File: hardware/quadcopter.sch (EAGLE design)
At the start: 62 parts, among them J1 AVR_SPI_PRG_6NS, J2 HEADER-4POS-2X2-0.1IN-FEMALE-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, J3 HEADER-10POSTH-254X10, J4 HEADER-4POS-0.1IN-FEMALE-SMD-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, Q1 MOSFET-SI2302CDS-T1-E3CT-ND, Q2 MOSFET-SI2302CDS-T1-E3CT-ND, Q3 MOSFET-SI2302CDS-T1-E3CT-ND, Q4 MOSFET-SI2302CDS-T1-E3CT-ND, Q5 MOSFET-SI2302CDS-T1-E3CT-ND, Q6 MOSFET-SI2302CDS-T1-E3CT-ND, SW1 PUSHBUTTON_SMD-VERTICAL-1, U1 ATMEGA128RFA1, U2 LSM-IMU-497-18367-1-NDIMU, Y1 CRYSTAL5X3

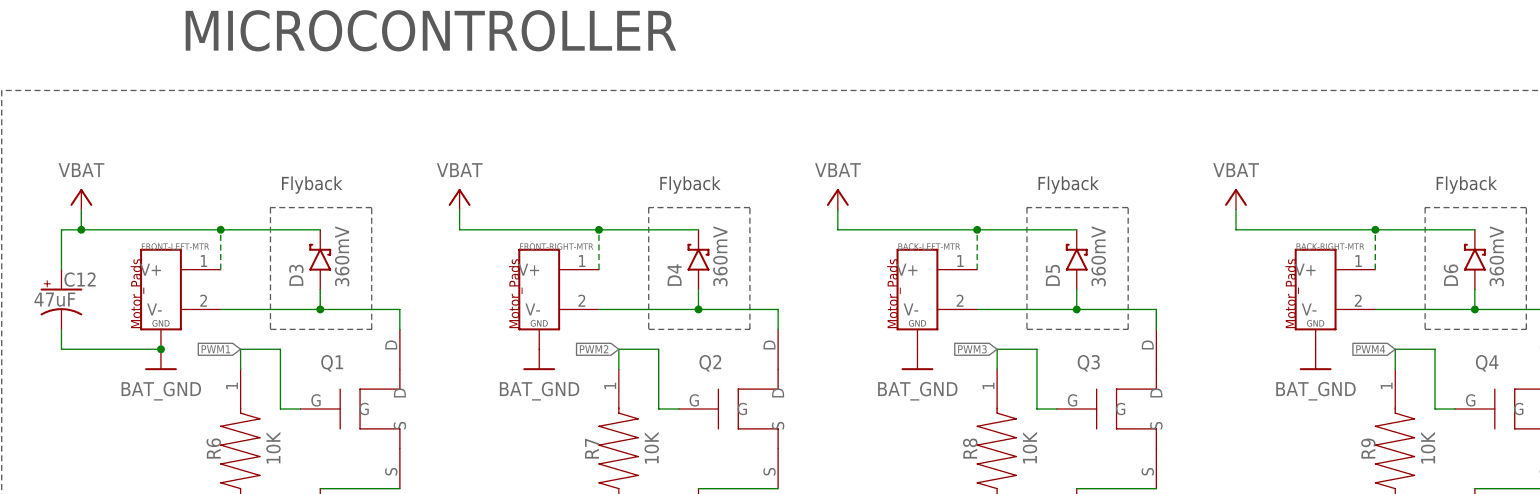
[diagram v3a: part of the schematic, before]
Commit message: renamed motor pads because mosfet is complaining?
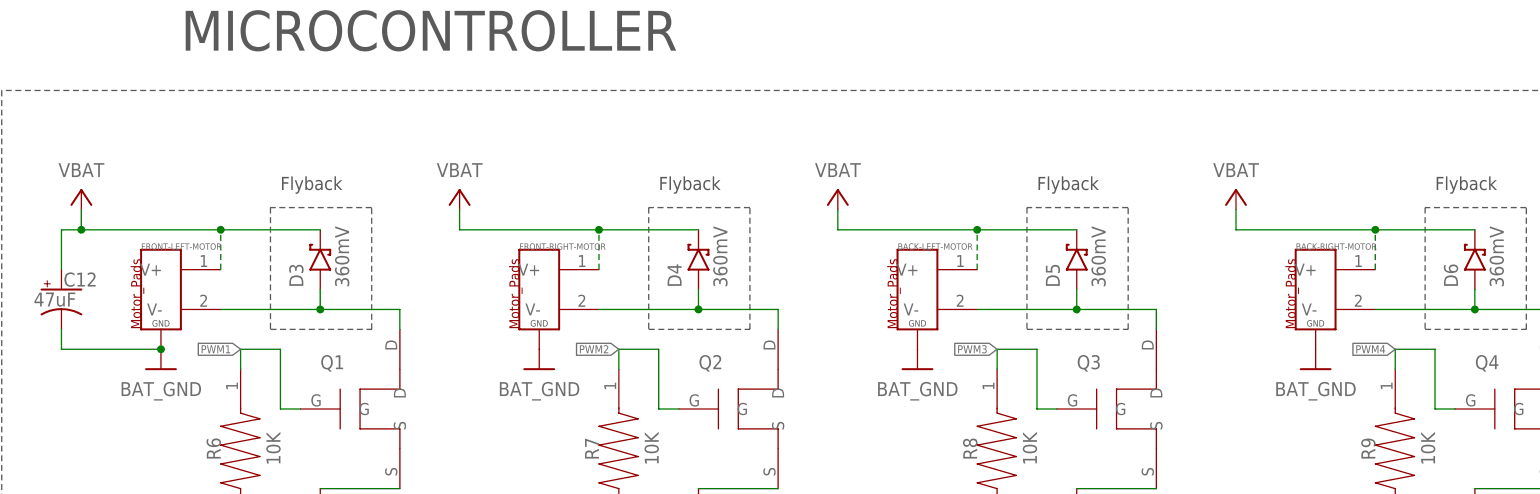
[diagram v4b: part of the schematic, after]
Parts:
- renumbered BACK-LEFT-MTR to BACK-LEFT-MOTOR, BACK-RIGHT-MTR to BACK-RIGHT-MOTOR, FRONT-LEFT-MTR to FRONT-LEFT-MOTOR, FRONT-RIGHT-MTR to FRONT-RIGHT-MOTOR
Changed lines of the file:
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@@
 <part name="GND18" library="quadparts_prebuilt_2022" deviceset="GND" device=""/>
 <part name="P+7" library="quadparts_prebuilt_2022" deviceset="3V" device=""/>
-<part name="FRONT-LEFT-MTR" library="quadparts_prebuilt_2022" deviceset="MOTOR_PADS_GND" device="-MOLEX-SMD"/>
+<part name="FRONT-LEFT-MOTOR" library="quadparts_prebuilt_2022" deviceset="MOTOR_PADS_GND" device="-MOLEX-SMD"/>
 <part name="P+8" library="quadparts_prebuilt_2022" deviceset="VBAT" device=""/>
 <part name="D3" library="quadparts_prebuilt_2022" deviceset="DIODE-SCHOTTKY_" device="-SMD-SOD123" package3d_urn="urn:adsk.eagle:package:11793366/1" value="360mV"/>
@@
 <part name="GND22" library="quadparts_prebuilt_2022" deviceset="GND" device=""/>
 <part name="Q1" library="custom_.lbr" library_urn="urn:adsk.wipprod:fs.file:vf.FjMADskDQ2Se9fX1PD5xcw" deviceset="MOSFET" device="-SI2302CDS-T1-E3CT-ND"/>
-<part name="FRONT-RIGHT-MTR" library="quadparts_prebuilt_2022" deviceset="MOTOR_PADS_GND" device="-MOLEX-SMD"/>
+<part name="FRONT-RIGHT-MOTOR" library="quadparts_prebuilt_2022" deviceset="MOTOR_PADS_GND" device="-MOLEX-SMD"/>
 <part name="P+9" library="quadparts_prebuilt_2022" deviceset="VBAT" device=""/>
 <part name="D4" library="quadparts_prebuilt_2022" deviceset="DIODE-SCHOTTKY_" device="-SMD-SOD123" package3d_urn="urn:adsk.eagle:package:11793366/1" value="360mV"/>
@@
 <part name="GND25" library="quadparts_prebuilt_2022" deviceset="GND" device=""/>
 <part name="Q2" library="custom_.lbr" library_urn="urn:adsk.wipprod:fs.file:vf.FjMADskDQ2Se9fX1PD5xcw" deviceset="MOSFET" device="-SI2302CDS-T1-E3CT-ND"/>
-<part name="BACK-LEFT-MTR" library="quadparts_prebuilt_2022" deviceset="MOTOR_PADS_GND" device="-MOLEX-SMD"/>
+<part name="BACK-LEFT-MOTOR" library="quadparts_prebuilt_2022" deviceset="MOTOR_PADS_GND" device="-MOLEX-SMD"/>
 <part name="P+10" library="quadparts_prebuilt_2022" deviceset="VBAT" device=""/>
 <part name="D5" library="quadparts_prebuilt_2022" deviceset="DIODE-SCHOTTKY_" device="-SMD-SOD123" package3d_urn="urn:adsk.eagle:package:11793366/1" value="360mV"/>
@@
 <part name="GND28" library="quadparts_prebuilt_2022" deviceset="GND" device=""/>
 <part name="Q3" library="custom_.lbr" library_urn="urn:adsk.wipprod:fs.file:vf.FjMADskDQ2Se9fX1PD5xcw" deviceset="MOSFET" device="-SI2302CDS-T1-E3CT-ND"/>
-<part name="BACK-RIGHT-MTR" library="quadparts_prebuilt_2022" deviceset="MOTOR_PADS_GND" device="-MOLEX-SMD"/>
+<part name="BACK-RIGHT-MOTOR" library="quadparts_prebuilt_2022" deviceset="MOTOR_PADS_GND" device="-MOLEX-SMD"/>
 <part name="P+11" library="quadparts_prebuilt_2022" deviceset="VBAT" device=""/>
 <part name="D6" library="quadparts_prebuilt_2022" deviceset="DIODE-SCHOTTKY_" device="-SMD-SOD123" package3d_urn="urn:adsk.eagle:package:11793366/1" value="360mV"/>
@@
 <attribute name="VALUE" x="287.02" y="162.56" size="1.778" layer="96" rot="R180" align="center"/>
 </instance>
-<instance part="FRONT-LEFT-MTR" gate="G$1" x="7.62" y="27.94" smashed="yes">
+<instance part="FRONT-LEFT-MOTOR" gate="G$1" x="7.62" y="27.94" smashed="yes">
 <attribute name="NAME" x="5.08" y="35.56" size="0.8128" layer="95"/>
 </instance>
@@
 <attribute name="NAME" x="27.94" y="20.32" size="1.778" layer="95"/>
 </instance>
-<instance part="FRONT-RIGHT-MTR" gate="G$1" x="55.88" y="27.94" smashed="yes">
+<instance part="FRONT-RIGHT-MOTOR" gate="G$1" x="55.88" y="27.94" smashed="yes">
 <attribute name="NAME" x="53.34" y="35.56" size="0.8128" layer="95"/>
 </instance>
@@
 <attribute name="NAME" x="76.2" y="20.32" size="1.778" layer="95"/>
 </instance>
-<instance part="BACK-LEFT-MTR" gate="G$1" x="104.14" y="27.94" smashed="yes">
+<instance part="BACK-LEFT-MOTOR" gate="G$1" x="104.14" y="27.94" smashed="yes">
 <attribute name="NAME" x="101.6" y="35.56" size="0.8128" layer="95"/>
 </instance>
@@
 <attribute name="NAME" x="124.46" y="20.32" size="1.778" layer="95"/>
 </instance>
-<instance part="BACK-RIGHT-MTR" gate="G$1" x="154.94" y="27.94" smashed="yes">
+<instance part="BACK-RIGHT-MOTOR" gate="G$1" x="154.94" y="27.94" smashed="yes">
 <attribute name="NAME" x="152.4" y="35.56" size="0.8128" layer="95"/>
 </instance>
@@
 <net name="VBAT" class="0">
 <segment>
-<pinref part="FRONT-LEFT-MTR" gate="G$1" pin="V+"/>
+<pinref part="FRONT-LEFT-MOTOR" gate="G$1" pin="V+"/>
 <wire x1="15.24" y1="33.02" x2="15.24" y2="38.1" width="0.1524" layer="91" style="longdash"/>
 <wire x1="15.24" y1="38.1" x2="-2.54" y2="38.1" width="0.1524" layer="91"/>
@@
 </segment>
 <segment>
-<pinref part="FRONT-RIGHT-MTR" gate="G$1" pin="V+"/>
+<pinref part="FRONT-RIGHT-MOTOR" gate="G$1" pin="V+"/>
 <wire x1="63.5" y1="33.02" x2="63.5" y2="38.1" width="0.1524" layer="91" style="longdash"/>
 <wire x1="63.5" y1="38.1" x2="45.72" y2="38.1" width="0.1524" layer="91"/>
@@
 </segment>
 <segment>
-<pinref part="BACK-LEFT-MTR" gate="G$1" pin="V+"/>
+<pinref part="BACK-LEFT-MOTOR" gate="G$1" pin="V+"/>
 <wire x1="111.76" y1="33.02" x2="111.76" y2="38.1" width="0.1524" layer="91" style="longdash"/>
 <wire x1="111.76" y1="38.1" x2="93.98" y2="38.1" width="0.1524" layer="91"/>
@@
 </segment>
 <segment>
-<pinref part="BACK-RIGHT-MTR" gate="G$1" pin="V+"/>
+<pinref part="BACK-RIGHT-MOTOR" gate="G$1" pin="V+"/>
 <wire x1="162.56" y1="33.02" x2="162.56" y2="38.1" width="0.1524" layer="91" style="longdash"/>
 <wire x1="162.56" y1="38.1" x2="144.78" y2="38.1" width="0.1524" layer="91"/>
@@
 <wire x1="27.94" y1="30.48" x2="27.94" y2="27.94" width="0.1524" layer="91"/>
 <wire x1="27.94" y1="27.94" x2="15.24" y2="27.94" width="0.1524" layer="91"/>
-<pinref part="FRONT-LEFT-MTR" gate="G$1" pin="V-"/>
+<pinref part="FRONT-LEFT-MOTOR" gate="G$1" pin="V-"/>
 <wire x1="27.94" y1="27.94" x2="38.1" y2="27.94" width="0.1524" layer="91"/>
 <junction x="27.94" y="27.94"/>
@@
 <net name="BAT_GND" class="0">
 <segment>
-<pinref part="FRONT-LEFT-MTR" gate="G$1" pin="GND"/>
+<pinref part="FRONT-LEFT-MOTOR" gate="G$1" pin="GND"/>
 <pinref part="GND20" gate="1" pin="BAT_GND"/>
 <wire x1="-5.08" y1="25.4" x2="-5.08" y2="22.86" width="0.1524" layer="91"/>
@@
 </segment>
 <segment>
-<pinref part="FRONT-RIGHT-MTR" gate="G$1" pin="GND"/>
+<pinref part="FRONT-RIGHT-MOTOR" gate="G$1" pin="GND"/>
 <pinref part="GND23" gate="1" pin="BAT_GND"/>
 </segment>
@@
 </segment>
 <segment>
-<pinref part="BACK-LEFT-MTR" gate="G$1" pin="GND"/>
+<pinref part="BACK-LEFT-MOTOR" gate="G$1" pin="GND"/>
 <pinref part="GND26" gate="1" pin="BAT_GND"/>
 </segment>
@@
 </segment>
 <segment>
-<pinref part="BACK-RIGHT-MTR" gate="G$1" pin="GND"/>
+<pinref part="BACK-RIGHT-MOTOR" gate="G$1" pin="GND"/>
 <pinref part="GND29" gate="1" pin="BAT_GND"/>
 </segment>
@@
 <wire x1="76.2" y1="30.48" x2="76.2" y2="27.94" width="0.1524" layer="91"/>
 <wire x1="76.2" y1="27.94" x2="63.5" y2="27.94" width="0.1524" layer="91"/>
-<pinref part="FRONT-RIGHT-MTR" gate="G$1" pin="V-"/>
+<pinref part="FRONT-RIGHT-MOTOR" gate="G$1" pin="V-"/>
 <wire x1="76.2" y1="27.94" x2="86.36" y2="27.94" width="0.1524" layer="91"/>
 <junction x="76.2" y="27.94"/>
@@
 <wire x1="124.46" y1="30.48" x2="124.46" y2="27.94" width="0.1524" layer="91"/>
 <wire x1="124.46" y1="27.94" x2="111.76" y2="27.94" width="0.1524" layer="91"/>
-<pinref part="BACK-LEFT-MTR" gate="G$1" pin="V-"/>
+<pinref part="BACK-LEFT-MOTOR" gate="G$1" pin="V-"/>
 <wire x1="124.46" y1="27.94" x2="134.62" y2="27.94" width="0.1524" layer="91"/>
 <junction x="124.46" y="27.94"/>
@@
 <wire x1="175.26" y1="30.48" x2="175.26" y2="27.94" width="0.1524" layer="91"/>
 <wire x1="175.26" y1="27.94" x2="162.56" y2="27.94" width="0.1524" layer="91"/>
-<pinref part="BACK-RIGHT-MTR" gate="G$1" pin="V-"/>
+<pinref part="BACK-RIGHT-MOTOR" gate="G$1" pin="V-"/>
 <wire x1="175.26" y1="27.94" x2="185.42" y2="27.94" width="0.1524" layer="91"/>
 <junction x="175.26" y="27.94"/>

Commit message: removed 3 mosfets and motor pads
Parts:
- removed BACK-LEFT-MOTOR, BACK-RIGHT-MOTOR, FRONT-RIGHT-MOTOR: MOTOR_PADS_GND-MOLEX-SMD, quadparts_prebuilt_2022:MOTOR_PADS_GND-MOLEX-SMD
- removed Q2, Q3, Q4: MOSFET-SI2302CDS-T1-E3CT-ND, custom_.lbr:MOSFET-SI2302CDS-T1-E3CT-ND
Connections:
- net BAT_GND: no longer BACK-LEFT-MOTOR.GND, BACK-RIGHT-MOTOR.GND, FRONT-RIGHT-MOTOR.GND, Q2.S, Q3.S, Q4.S
- net N$15: no longer FRONT-RIGHT-MOTOR.V-, Q2.D
- net N$16: no longer BACK-LEFT-MOTOR.V-, Q3.D
- net N$17: no longer BACK-RIGHT-MOTOR.V-, Q4.D
- net PWM2: no longer Q2.G
- net PWM3: no longer Q3.G
- net PWM4: no longer Q4.G
- net VBAT: no longer BACK-LEFT-MOTOR.V+, BACK-RIGHT-MOTOR.V+, FRONT-RIGHT-MOTOR.V+
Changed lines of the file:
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@@
 <part name="GND22" library="quadparts_prebuilt_2022" deviceset="GND" device=""/>
 <part name="Q1" library="custom_.lbr" library_urn="urn:adsk.wipprod:fs.file:vf.FjMADskDQ2Se9fX1PD5xcw" deviceset="MOSFET" device="-SI2302CDS-T1-E3CT-ND"/>
-<part name="FRONT-RIGHT-MOTOR" library="quadparts_prebuilt_2022" deviceset="MOTOR_PADS_GND" device="-MOLEX-SMD"/>
 <part name="P+9" library="quadparts_prebuilt_2022" deviceset="VBAT" device=""/>
 <part name="D4" library="quadparts_prebuilt_2022" deviceset="DIODE-SCHOTTKY_" device="-SMD-SOD123" package3d_urn="urn:adsk.eagle:package:11793366/1" value="360mV"/>
@@
 <part name="GND24" library="quadparts_prebuilt_2022" deviceset="BAT_GND" device=""/>
 <part name="GND25" library="quadparts_prebuilt_2022" deviceset="GND" device=""/>
-<part name="Q2" library="custom_.lbr" library_urn="urn:adsk.wipprod:fs.file:vf.FjMADskDQ2Se9fX1PD5xcw" deviceset="MOSFET" device="-SI2302CDS-T1-E3CT-ND"/>
-<part name="BACK-LEFT-MOTOR" library="quadparts_prebuilt_2022" deviceset="MOTOR_PADS_GND" device="-MOLEX-SMD"/>
 <part name="P+10" library="quadparts_prebuilt_2022" deviceset="VBAT" device=""/>
 <part name="D5" library="quadparts_prebuilt_2022" deviceset="DIODE-SCHOTTKY_" device="-SMD-SOD123" package3d_urn="urn:adsk.eagle:package:11793366/1" value="360mV"/>
@@
 <part name="GND27" library="quadparts_prebuilt_2022" deviceset="BAT_GND" device=""/>
 <part name="GND28" library="quadparts_prebuilt_2022" deviceset="GND" device=""/>
-<part name="Q3" library="custom_.lbr" library_urn="urn:adsk.wipprod:fs.file:vf.FjMADskDQ2Se9fX1PD5xcw" deviceset="MOSFET" device="-SI2302CDS-T1-E3CT-ND"/>
-<part name="BACK-RIGHT-MOTOR" library="quadparts_prebuilt_2022" deviceset="MOTOR_PADS_GND" device="-MOLEX-SMD"/>
 <part name="P+11" library="quadparts_prebuilt_2022" deviceset="VBAT" device=""/>
 <part name="D6" library="quadparts_prebuilt_2022" deviceset="DIODE-SCHOTTKY_" device="-SMD-SOD123" package3d_urn="urn:adsk.eagle:package:11793366/1" value="360mV"/>
@@
 <part name="GND30" library="quadparts_prebuilt_2022" deviceset="BAT_GND" device=""/>
 <part name="GND31" library="quadparts_prebuilt_2022" deviceset="GND" device=""/>
-<part name="Q4" library="custom_.lbr" library_urn="urn:adsk.wipprod:fs.file:vf.FjMADskDQ2Se9fX1PD5xcw" deviceset="MOSFET" device="-SI2302CDS-T1-E3CT-ND"/>
 <part name="C12" library="quadparts_prebuilt_2022" deviceset="CAPACITOR-POL_" device="47UF-SMD-1206-TAJA" package3d_urn="urn:adsk.eagle:package:11793387/1" value="47uF"/>
 <part name="REG" library="quadparts_prebuilt_2022" deviceset="TPS73633-DBVT" device="3V" value="3V"/>
@@
 <attribute name="NAME" x="27.94" y="20.32" size="1.778" layer="95"/>
 </instance>
-<instance part="FRONT-RIGHT-MOTOR" gate="G$1" x="55.88" y="27.94" smashed="yes">
-<attribute name="NAME" x="53.34" y="35.56" size="0.8128" layer="95"/>
-</instance>
 <instance part="P+9" gate="VCC" x="45.72" y="43.18" smashed="yes">
 <attribute name="VALUE" x="45.72" y="45.72" size="1.778" layer="96" rot="R180" align="center"/>
@@
 <attribute name="VALUE" x="58.42" y="-5.08" size="1.778" layer="96" align="center"/>
 </instance>
-<instance part="Q2" gate="G$1" x="83.82" y="15.24" smashed="yes">
-<attribute name="NAME" x="76.2" y="20.32" size="1.778" layer="95"/>
-</instance>
-<instance part="BACK-LEFT-MOTOR" gate="G$1" x="104.14" y="27.94" smashed="yes">
-<attribute name="NAME" x="101.6" y="35.56" size="0.8128" layer="95"/>
-</instance>
 <instance part="P+10" gate="VCC" x="93.98" y="43.18" smashed="yes">
 <attribute name="VALUE" x="93.98" y="45.72" size="1.778" layer="96" rot="R180" align="center"/>
@@
 <attribute name="VALUE" x="106.68" y="-5.08" size="1.778" layer="96" align="center"/>
 </instance>
-<instance part="Q3" gate="G$1" x="132.08" y="15.24" smashed="yes">
-<attribute name="NAME" x="124.46" y="20.32" size="1.778" layer="95"/>
-</instance>
-<instance part="BACK-RIGHT-MOTOR" gate="G$1" x="154.94" y="27.94" smashed="yes">
-<attribute name="NAME" x="152.4" y="35.56" size="0.8128" layer="95"/>
-</instance>
 <instance part="P+11" gate="VCC" x="144.78" y="43.18" smashed="yes">
 <attribute name="VALUE" x="144.78" y="45.72" size="1.778" layer="96" rot="R180" align="center"/>
@@
 <instance part="GND31" gate="1" x="157.48" y="-2.54" smashed="yes">
 <attribute name="VALUE" x="157.48" y="-5.08" size="1.778" layer="96" align="center"/>
-</instance>
-<instance part="Q4" gate="G$1" x="182.88" y="15.24" smashed="yes">
-<attribute name="NAME" x="175.26" y="20.32" size="1.778" layer="95"/>
 </instance>
 <instance part="C12" gate="G$1" x="-5.08" y="30.48" smashed="yes">
@@
 </segment>
 <segment>
-<pinref part="FRONT-RIGHT-MOTOR" gate="G$1" pin="V+"/>
 <wire x1="63.5" y1="33.02" x2="63.5" y2="38.1" width="0.1524" layer="91" style="longdash"/>
 <wire x1="63.5" y1="38.1" x2="45.72" y2="38.1" width="0.1524" layer="91"/>
@@
 </segment>
 <segment>
-<pinref part="BACK-LEFT-MOTOR" gate="G$1" pin="V+"/>
 <wire x1="111.76" y1="33.02" x2="111.76" y2="38.1" width="0.1524" layer="91" style="longdash"/>
 <wire x1="111.76" y1="38.1" x2="93.98" y2="38.1" width="0.1524" layer="91"/>
@@
 </segment>
 <segment>
-<pinref part="BACK-RIGHT-MOTOR" gate="G$1" pin="V+"/>
 <wire x1="162.56" y1="33.02" x2="162.56" y2="38.1" width="0.1524" layer="91" style="longdash"/>
 <wire x1="162.56" y1="38.1" x2="144.78" y2="38.1" width="0.1524" layer="91"/>
@@
 </segment>
 <segment>
-<pinref part="FRONT-RIGHT-MOTOR" gate="G$1" pin="GND"/>
-<pinref part="GND23" gate="1" pin="BAT_GND"/>
-</segment>
-<segment>
-<pinref part="Q2" gate="G$1" pin="S"/>
 <wire x1="86.36" y1="5.08" x2="76.2" y2="5.08" width="0.1524" layer="91"/>
 <pinref part="GND24" gate="1" pin="BAT_GND"/>
 </segment>
 <segment>
-<pinref part="BACK-LEFT-MOTOR" gate="G$1" pin="GND"/>
-<pinref part="GND26" gate="1" pin="BAT_GND"/>
-</segment>
-<segment>
-<pinref part="Q3" gate="G$1" pin="S"/>
 <wire x1="134.62" y1="5.08" x2="124.46" y2="5.08" width="0.1524" layer="91"/>
 <pinref part="GND27" gate="1" pin="BAT_GND"/>
 </segment>
 <segment>
-<pinref part="BACK-RIGHT-MOTOR" gate="G$1" pin="GND"/>
-<pinref part="GND29" gate="1" pin="BAT_GND"/>
-</segment>
-<segment>
-<pinref part="Q4" gate="G$1" pin="S"/>
 <wire x1="185.42" y1="5.08" x2="175.26" y2="5.08" width="0.1524" layer="91"/>
 <pinref part="GND30" gate="1" pin="BAT_GND"/>
@@
 <net name="PWM2" class="0">
 <segment>
-<pinref part="Q2" gate="G$1" pin="G"/>
 <wire x1="73.66" y1="15.24" x2="71.12" y2="15.24" width="0.1524" layer="91"/>
 <wire x1="71.12" y1="15.24" x2="71.12" y2="22.86" width="0.1524" layer="91"/>
@@
 <wire x1="76.2" y1="30.48" x2="76.2" y2="27.94" width="0.1524" layer="91"/>
 <wire x1="76.2" y1="27.94" x2="63.5" y2="27.94" width="0.1524" layer="91"/>
-<pinref part="FRONT-RIGHT-MOTOR" gate="G$1" pin="V-"/>
 <wire x1="76.2" y1="27.94" x2="86.36" y2="27.94" width="0.1524" layer="91"/>
 <junction x="76.2" y="27.94"/>
 <wire x1="86.36" y1="27.94" x2="86.36" y2="25.4" width="0.1524" layer="91"/>
-<pinref part="Q2" gate="G$1" pin="D"/>
 <pinref part="D4" gate="G$1" pin="A"/>
 </segment>
@@
 <wire x1="124.46" y1="30.48" x2="124.46" y2="27.94" width="0.1524" layer="91"/>
 <wire x1="124.46" y1="27.94" x2="111.76" y2="27.94" width="0.1524" layer="91"/>
-<pinref part="BACK-LEFT-MOTOR" gate="G$1" pin="V-"/>
 <wire x1="124.46" y1="27.94" x2="134.62" y2="27.94" width="0.1524" layer="91"/>
+<wire x1="134.62" y1="27.94" x2="134.62" y2="25.4" width="0.1524" layer="91"/>
+<pinref part="D5" gate="G$1" pin="A"/>
 <junction x="124.46" y="27.94"/>
-<wire x1="134.62" y1="27.94" x2="134.62" y2="25.4" width="0.1524" layer="91"/>
-<pinref part="Q3" gate="G$1" pin="D"/>
-<pinref part="D5" gate="G$1" pin="A"/>
 </segment>
 </net>
@@
 <wire x1="175.26" y1="30.48" x2="175.26" y2="27.94" width="0.1524" layer="91"/>
 <wire x1="175.26" y1="27.94" x2="162.56" y2="27.94" width="0.1524" layer="91"/>
-<pinref part="BACK-RIGHT-MOTOR" gate="G$1" pin="V-"/>
 <wire x1="175.26" y1="27.94" x2="185.42" y2="27.94" width="0.1524" layer="91"/>
 <junction x="175.26" y="27.94"/>
 <wire x1="185.42" y1="27.94" x2="185.42" y2="25.4" width="0.1524" layer="91"/>
-<pinref part="Q4" gate="G$1" pin="D"/>
 <pinref part="D6" gate="G$1" pin="A"/>
 </segment>
@@
 <net name="PWM3" class="0">
 <segment>
-<pinref part="Q3" gate="G$1" pin="G"/>
 <wire x1="121.92" y1="15.24" x2="119.38" y2="15.24" width="0.1524" layer="91"/>
 <wire x1="119.38" y1="15.24" x2="119.38" y2="22.86" width="0.1524" layer="91"/>
@@
 <net name="PWM4" class="0">
 <segment>
-<pinref part="Q4" gate="G$1" pin="G"/>
 <wire x1="172.72" y1="15.24" x2="170.18" y2="15.24" width="0.1524" layer="91"/>
 <wire x1="170.18" y1="15.24" x2="170.18" y2="22.86" width="0.1524" layer="91"/>
